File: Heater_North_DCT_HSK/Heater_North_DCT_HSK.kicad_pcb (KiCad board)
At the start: 2 copper layers, 53.3 x 63.5 mm, 8 parts, among them J1 NHB1, J2 NHB2, J3 Heater North

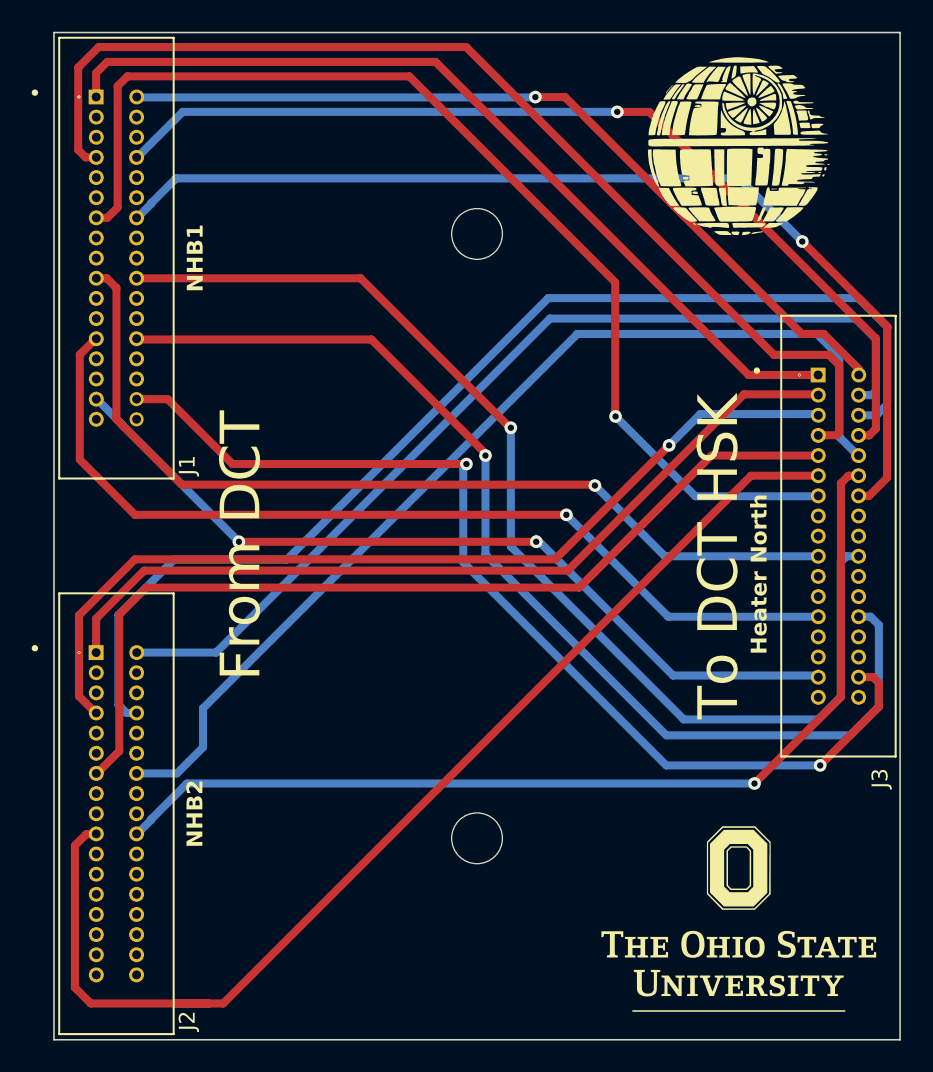
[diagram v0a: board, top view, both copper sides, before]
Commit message: New feedthrough PCBs to access spare heater channels for flowcontroller heaters.
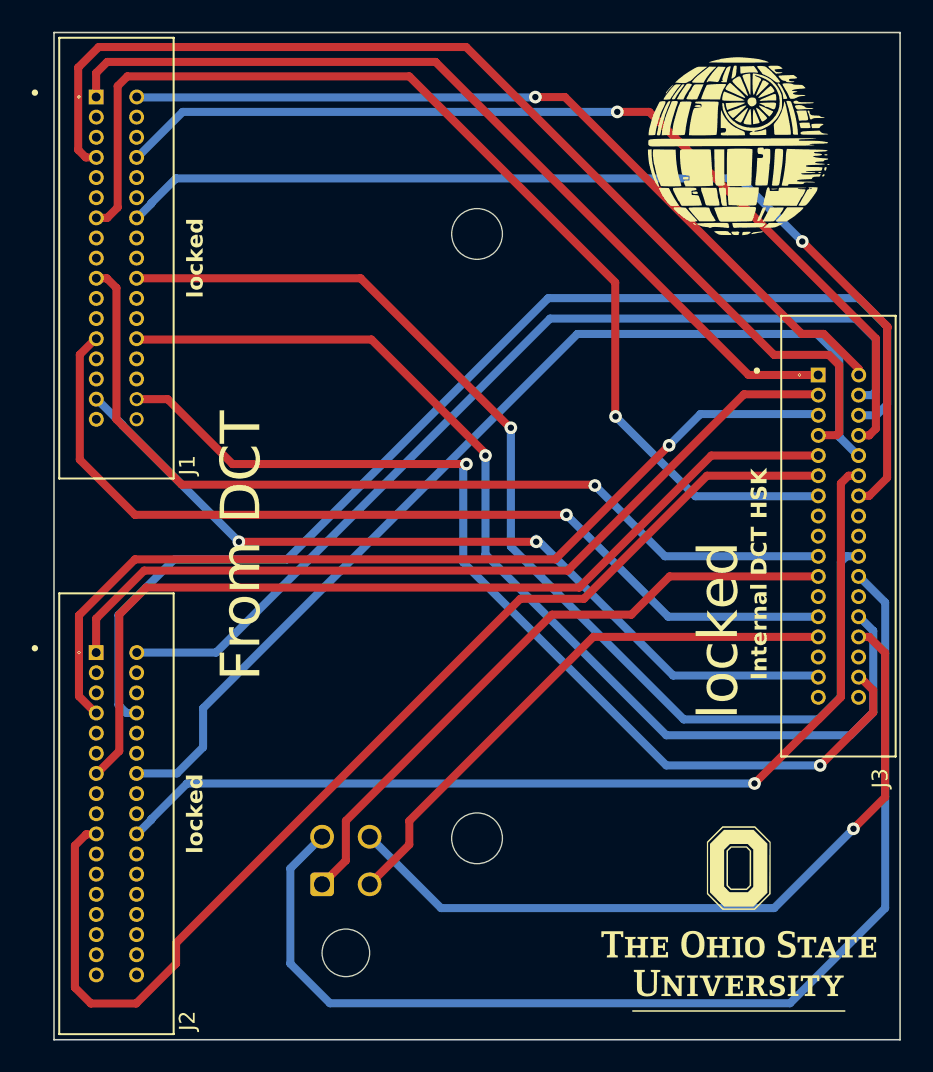
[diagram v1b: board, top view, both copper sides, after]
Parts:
- added J4: SparesN, Connector_Molex:Molex_Micro-Fit_3.0_43045-0400_2x02_P3.00mm_Horizontal, B.Cu at (118.5, 104.5)
- J1: value NHB1 -> locked
- J2: value NHB2 -> locked
- J3: value Heater North -> Internal DCT HSK
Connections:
- J3 pad 21: unconnected-(J3-Pin_21-Pad21) -> /SpareN1+
- J3 pad 22: unconnected-(J3-Pin_22-Pad22) -> /SpareN1-
- J3 pad 27: unconnected-(J3-Pin_27-Pad27) -> /SpareN2+
- J3 pad 28: unconnected-(J3-Pin_28-Pad28) -> /SpareN2-
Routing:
- net /SpareN1-: track 0.00 -> 71.5 mm
- net /SpareN2-: track 0.00 -> 48.4 mm, vias 0 -> 1
- net /SpareN1+: track 0.00 -> 40.8 mm
- net /SpareN2+: track 0.00 -> 35.6 mm
- net /HB2_19: track 73.8 -> 72.4 mm
- net /HB1_32: track 64.6 -> 63.9 mm
- net /HB1_26: track 68.3 -> 67.6 mm
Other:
- board text added: "locked"
- board text removed: "To DCT HSK"

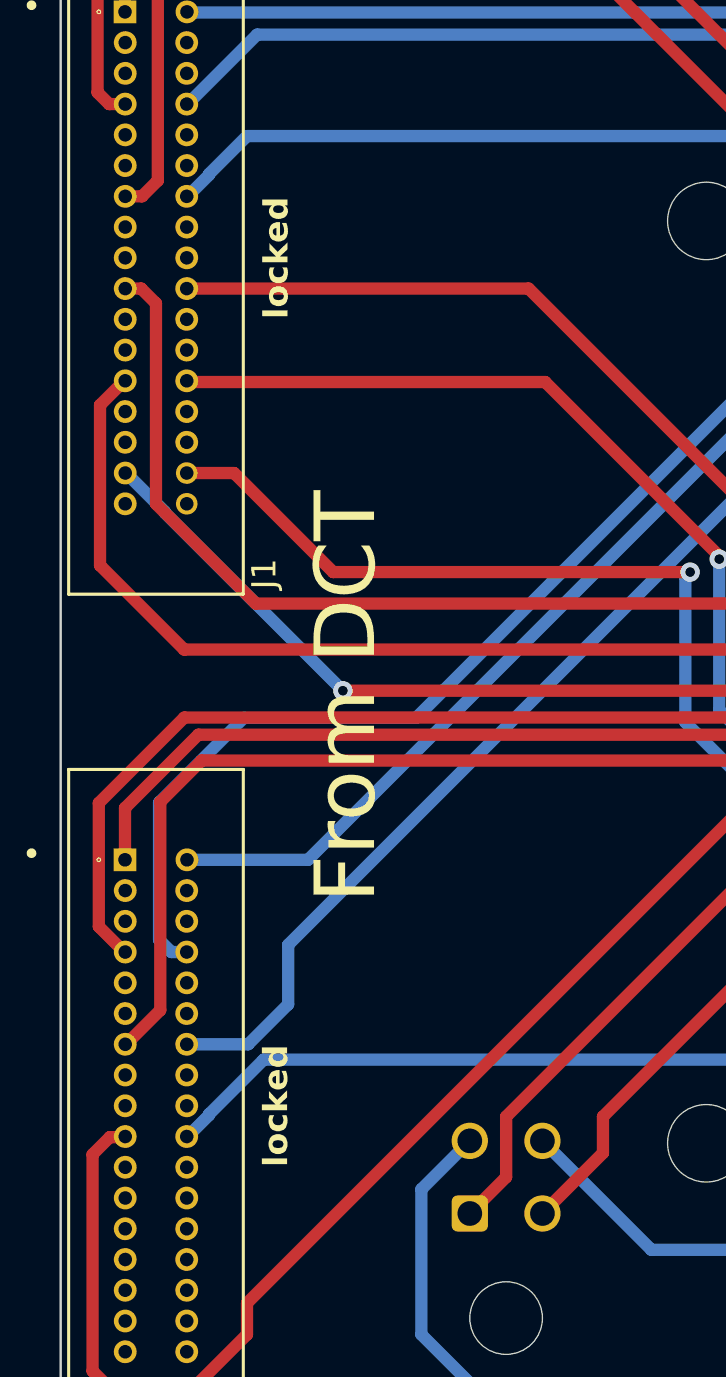
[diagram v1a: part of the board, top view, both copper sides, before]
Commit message: Files fabbed and tested. These work for the new version of the heater driver PCB.
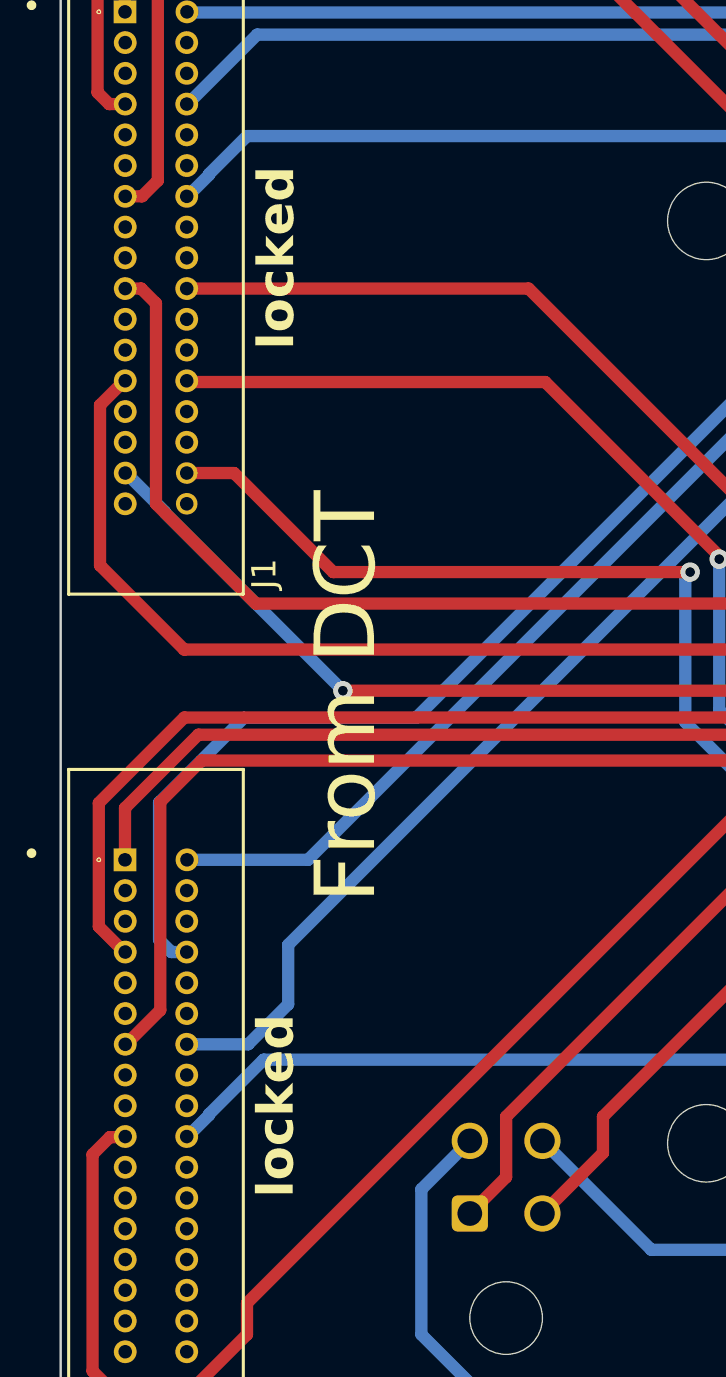
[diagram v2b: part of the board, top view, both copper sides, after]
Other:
- board text added: "Heater North Rev C Dennis H. Calderon 10/17/2023"
- board text removed: "Heater North Rev B Dennis H. Calderon 09/09/2023"
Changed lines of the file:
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@@
       (drillshape 0)
       (scaleselection 1)
-      (outputdirectory "Fab/Rev_B/")
+      (outputdirectory "Fab/Rev_C/")
     )
   )
@@
     )
     (fp_text value locked "NHB2" (at 0.000001 -4.953 90) (layer "F.SilkS")
-        (effects (font (size 1 1) (thickness 0.2) bold))
+        (effects (font (size 1.5 1.5) (thickness 0.375) bold))
     )
     (fp_line (start -13.894 -3.607) (end 13.894 -3.607)
@@
     )
     (fp_text value locked "NHB1" (at 0.000001 -4.97 90) (layer "F.SilkS")
-        (effects (font (size 1 1) (thickness 0.2) bold))
+        (effects (font (size 1.5 1.5) (thickness 0.375) bold))
     )
     (fp_line (start -13.894 -3.607) (end 13.894 -3.607)
@@
     (property "ki_keywords" "connector")
     (attr through_hole)
-    (fp_text reference "J4" (at 1.5 10.12) (layer "B.SilkS")
+    (fp_text reference "J4" (at 8.5 3.5) (layer "B.SilkS")
         (effects (font (size 1 1) (thickness 0.15)) (justify mirror))
     )
@@
       (stroke (width 0.1) (type solid)) (layer "B.Fab"))
     (pad "" np_thru_hole circle (at 1.5 4.32) (size 3 3) (drill 3) (layers "*.Cu" "*.Mask"))
-    (pad "1" thru_hole roundrect (at 0 0) (size 1.5 1.5) (drill 1.02) (layers "*.Cu" "*.Mask") (roundrect_rratio 0.166667)
+    (pad "1" thru_hole roundrect (at 0 0) (size 1.5 1.5) (drill 1.02) (layers "*.Cu" "*.Mask") (roundrect_rratio 0.1666673333)
       (net 73 "/SpareN1+") (pinfunction "Pin_1") (pintype "passive"))
     (pad "2" thru_hole circle (at 3 0) (size 1.5 1.5) (drill 1.02) (layers "*.Cu" "*.Mask")
@@
     (effects (font (size 3.5 3.5) (thickness 0.5)) (justify right bottom mirror))
   )
-  (gr_text "Heater North Rev B\nDennis H. Calderon\n09/09/2023" (at 144.772051 106.68811) (layer "B.SilkS")
+  (gr_text "Heater North Rev C\nDennis H. Calderon\n10/17/2023" (at 144.772051 106.68811) (layer "B.SilkS")
     (effects (font (size 1.3 1.3) (thickness 0.3) bold) (justify mirror))
   )
